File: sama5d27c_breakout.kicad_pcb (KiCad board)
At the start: 4 copper layers, 65 parts, among them U1 SAMA5D2x-SIP

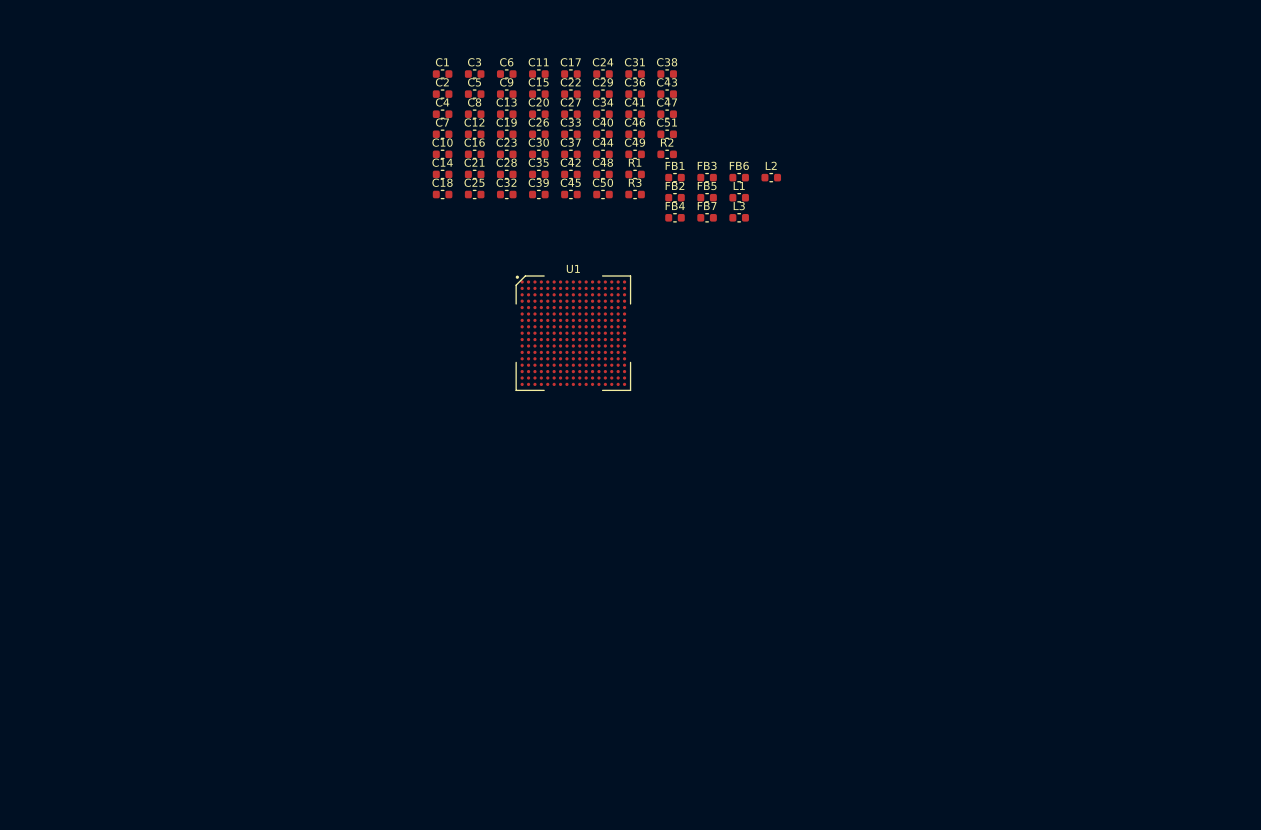
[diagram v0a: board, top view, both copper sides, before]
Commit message: Finish schematic (?), set footprints and start placement
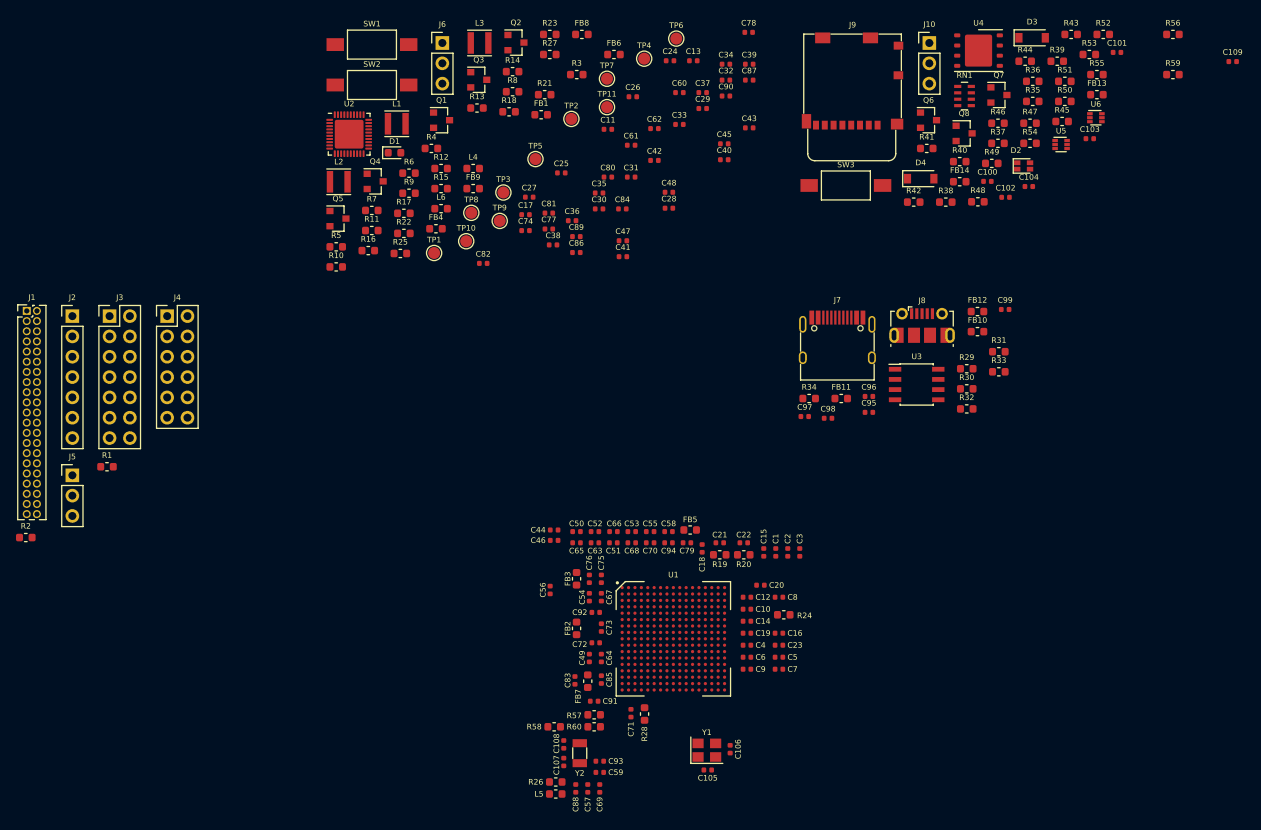
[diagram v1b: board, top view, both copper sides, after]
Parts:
- added C100: 0.1uF, Capacitor_SMD:C_0402_1005Metric, F.Cu at (203.8, 73.5)
- added C101: 10nF, Capacitor_SMD:C_0402_1005Metric, F.Cu at (220.0, 57.4)
- added C102: 10nF, Capacitor_SMD:C_0402_1005Metric, F.Cu at (206.0, 75.5)
- added C103: 10uF, Capacitor_SMD:C_0402_1005Metric, F.Cu at (216.6, 68.2)
- added C104: 10uF, Capacitor_SMD:C_0402_1005Metric, F.Cu at (208.9, 74.2)
- added C105: 12pF, Capacitor_SMD:C_0402_1005Metric, F.Cu at (168.8, 147.1)
- added C106: 12pF, Capacitor_SMD:C_0402_1005Metric, F.Cu at (171.6, 144.5)
- added C107: 12pF, Capacitor_SMD:C_0402_1005Metric, F.Cu at (150.8, 146.1)
- added C108: 12pF, Capacitor_SMD:C_0402_1005Metric, F.Cu at (150.8, 143.9)
- added C109: 10pF, Capacitor_SMD:C_0402_1005Metric, F.Cu at (234.4, 58.5)
- added C52: 1nF, Capacitor_SMD:C_0402_1005Metric, F.Cu at (154.7, 117.3)
- added C53: 1nF, Capacitor_SMD:C_0402_1005Metric, F.Cu at (159.3, 117.3)
- added C54: 1nF, Capacitor_SMD:C_0402_1005Metric, F.Cu at (154.0, 125.5)
- added C55: 1nF, Capacitor_SMD:C_0402_1005Metric, F.Cu at (161.6, 117.3)
- added C56: 10uF, Capacitor_SMD:C_0402_1005Metric, F.Cu at (149.1, 124.6)
- added C57: 1nF, Capacitor_SMD:C_0402_1005Metric, F.Cu at (153.8, 149.4)
- added C58: 1nF, Capacitor_SMD:C_0402_1005Metric, F.Cu at (163.9, 117.3)
- added C59: 1nF, Capacitor_SMD:C_0402_1005Metric, F.Cu at (155.3, 147.4)
- added C60: 0.1uF, Capacitor_SMD:C_0402_1005Metric, F.Cu at (165.3, 62.4)
- added C61: 0.1uF, Capacitor_SMD:C_0402_1005Metric, F.Cu at (159.2, 69.0)
- added C62: 0.1uF, Capacitor_SMD:C_0402_1005Metric, F.Cu at (162.1, 66.9)
- added C63: 0.1uF, Capacitor_SMD:C_0402_1005Metric, F.Cu at (154.7, 118.7)
- added C64: 0.1uF, Capacitor_SMD:C_0402_1005Metric, F.Cu at (155.5, 133.1)
- added C65: 0.1uF, Capacitor_SMD:C_0402_1005Metric, F.Cu at (152.4, 118.7)
- added C66: 0.1uF, Capacitor_SMD:C_0402_1005Metric, F.Cu at (157.0, 117.3)
- added C67: 0.1uF, Capacitor_SMD:C_0402_1005Metric, F.Cu at (155.5, 125.5)
- added C68: 0.1uF, Capacitor_SMD:C_0402_1005Metric, F.Cu at (159.3, 118.7)
- added C69: 0.1uF, Capacitor_SMD:C_0402_1005Metric, F.Cu at (155.3, 149.4)
- added C70: 0.1uF, Capacitor_SMD:C_0402_1005Metric, F.Cu at (161.6, 118.7)
- added C71: 0.1uF, Capacitor_SMD:C_0402_1005Metric, F.Cu at (159.2, 140.0)
- added C72: 0.1uF, Capacitor_SMD:C_0402_1005Metric, F.Cu at (154.8, 131.2)
- added C73: 0.1uF, Capacitor_SMD:C_0402_1005Metric, F.Cu at (155.5, 129.3)
- added C74: 0.1uF, Capacitor_SMD:C_0402_1005Metric, F.Cu at (146.0, 79.7)
- added C75: 0.1uF, Capacitor_SMD:C_0402_1005Metric, F.Cu at (155.5, 123.2)
- added C76: 0.1uF, Capacitor_SMD:C_0402_1005Metric, F.Cu at (154.0, 123.2)
- added C77: 0.1uF, Capacitor_SMD:C_0402_1005Metric, F.Cu at (148.9, 79.5)
- added C78: 0.1uF, Capacitor_SMD:C_0402_1005Metric, F.Cu at (173.9, 54.9)
- added C79: 0.1uF, Capacitor_SMD:C_0402_1005Metric, F.Cu at (166.2, 118.7)
- added C80: 0.1uF, Capacitor_SMD:C_0402_1005Metric, F.Cu at (156.3, 73.0)
- added C81: 0.1uF, Capacitor_SMD:C_0402_1005Metric, F.Cu at (148.9, 77.5)
- added C82: 4.7uF, Capacitor_SMD:C_0402_1005Metric, F.Cu at (140.7, 83.8)
- added C83: 0.1uF, Capacitor_SMD:C_0402_1005Metric, F.Cu at (152.2, 135.9)
- added C84: 4.7uF, Capacitor_SMD:C_0402_1005Metric, F.Cu at (158.1, 77.0)
- added C85: 0.1uF, Capacitor_SMD:C_0402_1005Metric, F.Cu at (155.5, 135.8)
- added C86: 0.1uF, Capacitor_SMD:C_0402_1005Metric, F.Cu at (152.4, 82.4)
- added C87: 0.1uF, Capacitor_SMD:C_0402_1005Metric, F.Cu at (174.0, 60.9)
- added C88: 4.7uF, Capacitor_SMD:C_0402_1005Metric, F.Cu at (152.3, 149.4)
- added C89: 0.1uF, Capacitor_SMD:C_0402_1005Metric, F.Cu at (152.4, 80.4)
- added C90: 4.7uF, Capacitor_SMD:C_0402_1005Metric, F.Cu at (171.1, 62.9)
- added C91: 0.1uF, Capacitor_SMD:C_0402_1005Metric, F.Cu at (154.6, 138.5)
- added C92: 0.1uF, Capacitor_SMD:C_0402_1005Metric, F.Cu at (154.8, 127.4)
- added C93: 0.1uF, Capacitor_SMD:C_0402_1005Metric, F.Cu at (155.3, 146.0)
- added C94: 0.1uF, Capacitor_SMD:C_0402_1005Metric, F.Cu at (163.9, 118.7)
- added C95: 20pF, Capacitor_SMD:C_0402_1005Metric, F.Cu at (188.9, 102.4)
- added C96: 0.1uF, Capacitor_SMD:C_0402_1005Metric, F.Cu at (188.9, 100.4)
- added C97: 0.1uF, Capacitor_SMD:C_0402_1005Metric, F.Cu at (180.9, 102.9)
- added C98: 10uF, Capacitor_SMD:C_0402_1005Metric, F.Cu at (183.8, 103.1)
- added C99: 0.1uF, Capacitor_SMD:C_0402_1005Metric, F.Cu at (206.0, 89.5)
- added D1: LED_CHARGE, LED_SMD:LED_0603_1608Metric, F.Cu at (129.6, 69.9)
- added D2: LED_ARGB, LED_SMD_Extra:LED_RGB_0606_1616Metric, F.Cu at (208.3, 71.6)
- added D3: 1N4148W, Diode_SMD:D_SOD-123, F.Cu at (209.3, 55.6)
- added D4: 1N4148W, Diode_SMD:D_SOD-123, F.Cu at (195.4, 73.2)
- added FB10: BLM18PG300SN1D, Inductor_SMD:L_0603_1608Metric, F.Cu at (202.5, 92.3)
- added FB11: BLM18PG300SN1D, Inductor_SMD:L_0603_1608Metric, F.Cu at (185.5, 100.7)
- added FB12: BLM18PG300SN1D, Inductor_SMD:L_0603_1608Metric, F.Cu at (202.5, 89.8)
- added FB13: BLM18PG300SN1D, Inductor_SMD:L_0603_1608Metric, F.Cu at (217.4, 62.7)
- added FB14: BLM18PG300SN1D, Inductor_SMD:L_0603_1608Metric, F.Cu at (200.3, 73.6)
- added FB8: BLM18PG300SN1D, Inductor_SMD:L_0603_1608Metric, F.Cu at (153.1, 55.2)
- added FB9: BLM18PG300SN1D, Inductor_SMD:L_0603_1608Metric, F.Cu at (139.5, 74.4)
- added J1: Conn_LCD, Connector_PinHeader_1.27mm:PinHeader_2x21_P1.27mm_Vertical, F.Cu at (83.7, 89.7)
- added J10: Conn_Speaker, Connector_PinHeader_2.54mm:PinHeader_1x03_P2.54mm_Vertical, F.Cu at (196.5, 56.2)
- added J2: Conn_JTAG, Connector_PinHeader_2.54mm:PinHeader_1x07_P2.54mm_Vertical, F.Cu at (89.4, 90.4)
- added J3: Conn_SDMMC0, Connector_PinHeader_2.54mm:PinHeader_2x07_P2.54mm_Vertical, F.Cu at (94.0, 90.4)
- added J4: Conn_FLEXCOM3_4, Connector_PinHeader_2.54mm:PinHeader_2x06_P2.54mm_Vertical, F.Cu at (101.2, 90.4)
- added J5: Conn_DBGU, Connector_PinHeader_2.54mm:PinHeader_1x03_P2.54mm_Vertical, F.Cu at (89.4, 110.3)
- added J6: Conn_BAT, Connector_PinHeader_2.54mm:PinHeader_1x03_P2.54mm_Vertical, F.Cu at (135.6, 56.2)
- added J7: USB_C_Receptacle_USB2.0, Connector_USB_Extra:USB_C_Receptacle_GT-USB-7010, F.Cu at (185.0, 93.7)
- added J8: USB_B_Micro, Connector_USB:USB_Micro-B_Molex-105017-0001, F.Cu at (195.6, 91.5)
- added J9: Micro_SD_Card_Det, Connector_Card_Extra:microSD_HC_Molex_104031-0811, F.Cu at (186.9, 61.0)
- added L4: MLZ1608N100L, Inductor_SMD:L_0603_1608Metric, F.Cu at (139.5, 71.9)
- added L5: MLZ1608N100L, Inductor_SMD:L_0603_1608Metric, F.Cu at (149.8, 150.1)
- added L6: MLZ1608N100L, Inductor_SMD:L_0603_1608Metric, F.Cu at (135.5, 76.9)
- added Q1: BSS138, Package_TO_SOT_SMD:SOT-23, F.Cu at (135.5, 65.9)
- added Q2: BSS138, Package_TO_SOT_SMD:SOT-23, F.Cu at (144.8, 56.2)
- added Q3: BSS138, Package_TO_SOT_SMD:SOT-23, F.Cu at (140.2, 60.8)
- added Q4: BSS138, Package_TO_SOT_SMD:SOT-23, F.Cu at (127.2, 73.5)
- added Q5: BSS138, Package_TO_SOT_SMD:SOT-23, F.Cu at (122.6, 78.2)
- added Q6: BSS138, Package_TO_SOT_SMD:SOT-23, F.Cu at (196.4, 65.9)
- added Q7: BSS138, Package_TO_SOT_SMD:SOT-23, F.Cu at (205.2, 62.7)
- added Q8: BSS138, Package_TO_SOT_SMD:SOT-23, F.Cu at (200.8, 67.5)
- added R10: 100K, Resistor_SMD:R_0603_1608Metric, F.Cu at (122.4, 84.2)
- added R11: 10K, Resistor_SMD:R_0603_1608Metric, F.Cu at (126.8, 79.7)
- added R12: 10K, Resistor_SMD:R_0603_1608Metric, F.Cu at (135.5, 71.9)
- added R13: 49.9K, Resistor_SMD:R_0603_1608Metric, F.Cu at (140.0, 64.4)
- added R14: 2.43K, Resistor_SMD:R_0603_1608Metric, F.Cu at (144.4, 59.8)
- added R15: 100R, Resistor_SMD:R_0603_1608Metric, F.Cu at (135.5, 74.4)
- added R16: 100R, Resistor_SMD:R_0603_1608Metric, F.Cu at (126.4, 82.2)
- added R17: 100R, Resistor_SMD:R_0603_1608Metric, F.Cu at (130.8, 77.5)
- added R18: 10K, Resistor_SMD:R_0603_1608Metric, F.Cu at (144.0, 64.8)
- added R19: 1.5K, Resistor_SMD:R_0603_1608Metric, F.Cu at (170.3, 120.2)
- added R20: 1.5K, Resistor_SMD:R_0603_1608Metric, F.Cu at (173.3, 120.2)
- added R21: 100R, Resistor_SMD:R_0603_1608Metric, F.Cu at (148.4, 62.7)
- added R22: 2.2M, Resistor_SMD:R_0603_1608Metric, F.Cu at (130.8, 80.0)
- added R23: 1.5M, Resistor_SMD:R_0603_1608Metric, F.Cu at (149.1, 55.2)
- added R24: 0R, Resistor_SMD:R_0603_1608Metric, F.Cu at (178.3, 127.7)
- added R25: 2.2R, Resistor_SMD:R_0603_1608Metric, F.Cu at (130.4, 82.5)
- added R26: 2.2R, Resistor_SMD:R_0603_1608Metric, F.Cu at (149.8, 148.6)
- added R27: 2.2R, Resistor_SMD:R_0603_1608Metric, F.Cu at (149.1, 57.7)
- added R28: 0R, Resistor_SMD:R_0603_1608Metric, F.Cu at (160.9, 140.1)
- added R29: 5.1K, Resistor_SMD:R_0603_1608Metric, F.Cu at (201.2, 96.9)
- added R30: 5.1K, Resistor_SMD:R_0603_1608Metric, F.Cu at (201.2, 99.5)
- added R31: 100K, Resistor_SMD:R_0603_1608Metric, F.Cu at (205.2, 94.8)
- added R32: 200K, Resistor_SMD:R_0603_1608Metric, F.Cu at (201.2, 102.0)
- added R33: 10K, Resistor_SMD:R_0603_1608Metric, F.Cu at (205.2, 97.3)
- added R34: 10K, Resistor_SMD:R_0603_1608Metric, F.Cu at (181.5, 100.7)
- added R35: 10K, Resistor_SMD:R_0603_1608Metric, F.Cu at (209.4, 63.5)
- added R36: 10K, Resistor_SMD:R_0603_1608Metric, F.Cu at (209.4, 61.0)
- added R37: 100R, Resistor_SMD:R_0603_1608Metric, F.Cu at (205.1, 68.8)
- added R38: 10K, Resistor_SMD:R_0603_1608Metric, F.Cu at (198.6, 76.1)
- added R39: 27R, Resistor_SMD:R_0603_1608Metric, F.Cu at (212.5, 58.5)
- added R4: 100K, Resistor_SMD:R_0603_1608Metric, F.Cu at (134.3, 69.4)
- added R40: 27R, Resistor_SMD:R_0603_1608Metric, F.Cu at (200.3, 71.1)
- added R41: 27R, Resistor_SMD:R_0603_1608Metric, F.Cu at (196.2, 69.4)
- added R42: 27R, Resistor_SMD:R_0603_1608Metric, F.Cu at (194.5, 76.1)
- added R43: 27R, Resistor_SMD:R_0603_1608Metric, F.Cu at (214.2, 55.2)
- added R44: 27R, Resistor_SMD:R_0603_1608Metric, F.Cu at (208.5, 58.5)
- added R45: 10K, Resistor_SMD:R_0603_1608Metric, F.Cu at (213.1, 66.0)
- added R46: 27R, Resistor_SMD:R_0603_1608Metric, F.Cu at (205.1, 66.3)
- added R47: 27R, Resistor_SMD:R_0603_1608Metric, F.Cu at (209.1, 66.3)
- added R48: 27R, Resistor_SMD:R_0603_1608Metric, F.Cu at (202.6, 76.1)
- added R49: 27R, Resistor_SMD:R_0603_1608Metric, F.Cu at (204.3, 71.3)
- added R5: 100K, Resistor_SMD:R_0603_1608Metric, F.Cu at (122.4, 81.7)
- added R50: 10K, Resistor_SMD:R_0603_1608Metric, F.Cu at (213.4, 63.5)
- added R51: 0R, Resistor_SMD:R_0603_1608Metric, F.Cu at (213.4, 61.0)
- added R52: 10K, Resistor_SMD:R_0603_1608Metric, F.Cu at (218.2, 55.2)
- added R53: 10K, Resistor_SMD:R_0603_1608Metric, F.Cu at (216.5, 57.7)
- added R54: 10K, Resistor_SMD:R_0603_1608Metric, F.Cu at (209.1, 68.8)
- added R55: 10K, Resistor_SMD:R_0603_1608Metric, F.Cu at (217.4, 60.2)
- added R56: 100R, Resistor_SMD:R_0603_1608Metric, F.Cu at (226.9, 55.2)
- added R57: 100R, Resistor_SMD:R_0603_1608Metric, F.Cu at (154.6, 140.2)
- added R58: 10K, Resistor_SMD:R_0603_1608Metric, F.Cu at (149.6, 141.7)
- added R59: 5.62K, Resistor_SMD:R_0603_1608Metric, F.Cu at (226.9, 60.2)
- added R6: 68K, Resistor_SMD:R_0603_1608Metric, F.Cu at (131.5, 72.5)
- added R60: 100R, Resistor_SMD:R_0603_1608Metric, F.Cu at (154.6, 141.7)
- added R7: 1K, Resistor_SMD:R_0603_1608Metric, F.Cu at (126.8, 77.2)
- added R8: 100K, Resistor_SMD:R_0603_1608Metric, F.Cu at (144.4, 62.3)
- added R9: 49.9K, Resistor_SMD:R_0603_1608Metric, F.Cu at (131.5, 75.0)
- added RN1: 68K, Resistor_SMD:R_Array_Concave_4x0603, F.Cu at (200.9, 62.9)
- added SW1: SW_WAKEUP, Button_Switch_SMD:SW_SPST_FSMSM, F.Cu at (126.8, 56.4)
- added SW2: SW_RESET, Button_Switch_SMD:SW_SPST_FSMSM, F.Cu at (126.8, 61.5)
- added SW3: SW_USR, Button_Switch_SMD:SW_SPST_FSMSM, F.Cu at (186.1, 74.0)
- added TP1: TP_VBUS, TestPoint:TestPoint_Pad_D1.5mm, F.Cu at (134.6, 82.5)
- added TP10: TP_VDDBU, TestPoint:TestPoint_Pad_D1.5mm, F.Cu at (138.6, 81.0)
- added TP11: TP_VDDSDMMC, TestPoint:TestPoint_Pad_D1.5mm, F.Cu at (156.2, 64.2)
- added TP2: TP_5V, TestPoint:TestPoint_Pad_D1.5mm, F.Cu at (151.8, 65.7)
- added TP3: TP_1.35V, TestPoint:TestPoint_Pad_D1.5mm, F.Cu at (143.3, 74.9)
- added TP4: TP_1.2V, TestPoint:TestPoint_Pad_D1.5mm, F.Cu at (160.9, 58.2)
- added TP5: TP_3.3V, TestPoint:TestPoint_Pad_D1.5mm, F.Cu at (147.3, 70.7)
- added TP6: TP_VDDFUSE, TestPoint:TestPoint_Pad_D1.5mm, F.Cu at (164.9, 55.7)
- added TP7: TP_3.3VP, TestPoint:TestPoint_Pad_D1.5mm, F.Cu at (156.2, 60.7)
- added TP8: TP_VDD_LED, TestPoint:TestPoint_Pad_D1.5mm, F.Cu at (139.2, 77.5)
- added TP9: TP_VDDSDHC1V8, TestPoint:TestPoint_Pad_D1.5mm, F.Cu at (142.8, 78.5)
- added U2: ACT8945A, Package_DFN_QFN:QFN-40-1EP_5x5mm_P0.4mm_EP3.6x3.6mm, F.Cu at (124.0, 67.6)
- added U3: MIC2025, Package_SO:SOIC-8_3.9x4.9mm_P1.27mm, F.Cu at (194.9, 98.9)
- added U4: IS25LP128F, Package_SON:WSON-8-1EP_6x5mm_P1.27mm_EP3.4x4mm, F.Cu at (202.6, 57.2)
- added U5: DMC2450, Package_TO_SOT_SMD:SOT-563, F.Cu at (213.0, 68.9)
- added U6: DMC2450, Package_TO_SOT_SMD:SOT-563, F.Cu at (217.3, 65.6)
- added Y1: TSX-3225 24MHz, Crystal:Crystal_SMD_3225-4Pin_3.2x2.5mm, F.Cu at (168.7, 144.6)
- added Y2: 32kHz, Crystal:Crystal_SMD_3215-2Pin_3.2x1.5mm, F.Cu at (152.8, 145.0)
- C1, C13, C3: value 10uF -> 0.1uF; footprint Capacitor_SMD:C_0603_1608Metric -> Capacitor_SMD:C_0402_1005Metric
- C10, C11, C12, C14, C16, C2, C4, C5, C6, C7, C8, C9: value 1nF -> 0.1uF; footprint Capacitor_SMD:C_0603_1608Metric -> Capacitor_SMD:C_0402_1005Metric
- C15: value 1nF -> 2.2uF; footprint Capacitor_SMD:C_0603_1608Metric -> Capacitor_SMD:C_0402_1005Metric
- C17, C20, C24: value 0.1uF -> 2.2uF; footprint Capacitor_SMD:C_0603_1608Metric -> Capacitor_SMD:C_0402_1005Metric
- C18, C30, C31, C32, C33, C34: value 0.1uF -> 4.7uF; footprint Capacitor_SMD:C_0603_1608Metric -> Capacitor_SMD:C_0402_1005Metric
- C19, C21, C22, C23, C29, C37, C40, C43: footprint Capacitor_SMD:C_0603_1608Metric -> Capacitor_SMD:C_0402_1005Metric
- C25, C27, C28, C35, C36, C38, C42, C44, C46: value 0.1uF -> 10uF; footprint Capacitor_SMD:C_0603_1608Metric -> Capacitor_SMD:C_0402_1005Metric
- C26: value 0.1uF -> 47nF; footprint Capacitor_SMD:C_0603_1608Metric -> Capacitor_SMD:C_0402_1005Metric
- C39, C41: value 4.7uF -> 10uF; footprint Capacitor_SMD:C_0603_1608Metric -> Capacitor_SMD:C_0402_1005Metric
- C45, C47: value 4.7uF -> 1nF; footprint Capacitor_SMD:C_0603_1608Metric -> Capacitor_SMD:C_0402_1005Metric
- C48, C49, C50, C51: value 0.1uF -> 1nF; footprint Capacitor_SMD:C_0603_1608Metric -> Capacitor_SMD:C_0402_1005Metric
- FB1: value BLM03AX100SZ1 -> BLM18PG181SN1D
- FB2, FB3, FB4, FB5, FB6, FB7: value BLM03AX100SZ1 -> BLM18PG300SN1D
- L1, L2, L3: value MLZ1608N100L -> LQM2HPN2R2MG0L; footprint Inductor_SMD:L_0603_1608Metric -> Inductor_SMD:L_Taiyo-Yuden_MD-3030
- R1, R2: value 2.2R -> 4.7K
- R3: value 2.2R -> 100K
- moved R2 93.4 mm to (83.6, 118.0)
- moved C5 80.0 mm to (177.7, 133.0), turned to 180 degrees
- moved C7 79.0 mm to (177.7, 134.5), turned to 180 degrees
- moved C6 78.8 mm to (173.7, 133.0), turned to 180 degrees
- moved C9 77.9 mm to (173.7, 134.5), turned to 180 degrees
- moved C4 76.5 mm to (173.7, 131.5), turned to 180 degrees
- moved R1 75.4 mm to (93.7, 109.2)
- moved C1 72.9 mm to (177.3, 119.9), turned to 270 degrees
- moved C3 72.3 mm to (180.3, 119.9), turned to 270 degrees
- moved C2 71.7 mm to (178.8, 119.9), turned to 270 degrees
- moved C8 71.4 mm to (177.7, 125.5), turned to 180 degrees
- moved C16 70.9 mm to (177.7, 130.0), turned to 180 degrees
- moved C23 70.2 mm to (177.7, 131.5), turned to 180 degrees
- moved C19 69.2 mm to (173.7, 130.0), turned to 180 degrees
- moved C10 68.4 mm to (173.7, 127.0), turned to 180 degrees
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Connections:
- C1 pad 2: VDDIODDR -> +1V35
- C10 pad 2: VDDIODDR -> +1V35
- C11 pad 1: GND -> Net-(C11-Pad1)
- C11 pad 2: VDDCORE -> Net-(C11-Pad2)
- C12 pad 2: VDDIODDR -> +1V35
- C13 pad 1: GND -> +5V
- C13 pad 2: +3V3 -> Net-(C13-Pad2)
- C14 pad 2: VDDCORE -> +1V35
- C15 pad 2: VDDIODDR -> +1V35
- C16 pad 2: VDDCORE -> +1V35
- C17 pad 2: VDDIODDR -> +1V35
- C18 pad 1: GND -> +1V35
- C18 pad 2: VDDCORE -> GND
- C19 pad 2: VDDIODDR -> +1V35
- C2 pad 2: VDDIODDR -> +1V35
- C20 pad 2: VDDCORE -> +1V35
- C21 pad 1: GND -> Net-(C21-Pad1)
- C21 pad 2: VDDIODDR -> +1V35
- C22 pad 2: VDDCORE -> Net-(C21-Pad1)
- C23 pad 2: VDDIODDR -> +1V35
- C24 pad 2: VDDCORE -> +1V35
- C25 pad 1: GND -> VBUS
- C25 pad 2: VDDIODDR -> GND
- C26 pad 1: GND -> Net-(C26-Pad1)
- C26 pad 2: VDDCORE -> GND
- C27 pad 2: VDDIODDR -> +5V
- C28 pad 1: VDDBU -> GND
- C28 pad 2: GND -> +5V
- C29 pad 1: Net-(C29-Pad1) -> GND
- C29 pad 2: GND -> +5V
- C3 pad 2: VDDCORE -> +1V35
- C30 pad 1: Net-(C29-Pad1) -> GND
- C30 pad 2: GND -> +5V
- C31 pad 1: Net-(C29-Pad1) -> GND
- C31 pad 2: GND -> VDDFUSE
- C32 pad 1: Net-(C32-Pad1) -> GND
- C32 pad 2: GND -> +3.3VP
- C33 pad 1: Net-(C32-Pad1) -> GND
- C33 pad 2: GND -> /Power/VDD_LED
- C34 pad 1: Net-(C34-Pad1) -> GND
- C34 pad 2: GND -> /Power/VDDSDHC1V8
- C35 pad 1: Net-(C34-Pad1) -> GND
- C35 pad 2: GND -> +1V35
- C36 pad 1: Net-(C36-Pad1) -> GND
- C36 pad 2: GND -> +1V35
- C37 pad 1: Net-(C37-Pad1) -> GND
- C37 pad 2: GND -> +1V35
- C38 pad 1: VDDFUSE -> GND
- C38 pad 2: GND -> +1V2
- C39 pad 1: Net-(C39-Pad1) -> GND
- C39 pad 2: GND -> +1V2
- C4 pad 2: VDDIODDR -> +1V35
- C40 pad 1: Net-(C39-Pad1) -> GND
- C40 pad 2: GND -> +1V2
- C41 pad 1: Net-(C41-Pad1) -> GND
- C41 pad 2: GND -> +3V3
- C42 pad 1: Net-(C41-Pad1) -> GND
- C42 pad 2: GND -> +3V3
- C43 pad 1: Net-(C43-Pad1) -> GND
- C43 pad 2: GNDS -> +3V3
- C44 pad 1: VDDSDMMC -> GND
- C44 pad 2: GND -> +1V35
- C45 pad 1: Net-(C45-Pad1) -> GND
- C45 pad 2: GND -> +1V35
- C46 pad 1: Net-(C45-Pad1) -> GND
- C46 pad 2: GND -> +1V2
- C47 pad 1: Net-(C47-Pad1) -> GND
- C47 pad 2: GND -> +1V35
- C48 pad 1: Net-(C47-Pad1) -> GND
- C48 pad 2: GND -> +1V2
- C49 pad 1: VDDISC -> GND
- C49 pad 2: GND -> +1V35
- C5 pad 2: VDDCORE -> +1V35
- C50 pad 2: VDDCORE -> +1V2
- C51 pad 2: VDDIODDR -> +1V35
- C6 pad 2: VDDIODDR -> +1V35
- C7 pad 2: VDDCORE -> +1V35
- C8 pad 2: VDDIODDR -> +1V35
- C9 pad 2: VDDCORE -> +1V35
- FB1 pad 1: +3V3 -> Net-(FB1-Pad1)
- FB1 pad 2: Net-(C29-Pad1) -> /Power/VDDSDHC1V8
- FB2 pad 1: +3V3 -> +3.3VP
- FB2 pad 2: Net-(C32-Pad1) -> VDDA
- FB3 pad 2: Net-(C34-Pad1) -> Net-(C75-Pad1)
- FB4 pad 2: Net-(C36-Pad1) -> Net-(C77-Pad1)
- FB5 pad 1: VDDCORE -> +3V3
- FB5 pad 2: Net-(C37-Pad1) -> Net-(C79-Pad1)
- FB6 pad 1: VDDCORE -> +1V2
- FB6 pad 2: Net-(C41-Pad1) -> Net-(C80-Pad1)
- FB7 pad 1: +3V3 -> +1V2
- FB7 pad 2: Net-(C43-Pad1) -> Net-(C84-Pad1)
- L1 pad 1: Net-(L1-Pad1) -> +1V35
- L1 pad 2: Net-(C39-Pad1) -> Net-(L1-Pad2)
- L2 pad 1: Net-(L2-Pad1) -> +1V2
- L2 pad 2: Net-(C45-Pad1) -> Net-(L2-Pad2)
- L3 pad 1: Net-(L3-Pad1) -> +3V3
- L3 pad 2: Net-(C47-Pad1) -> Net-(L3-Pad2)
- R1 pad 1: Net-(L1-Pad1) -> +3V3
- R1 pad 2: +3V3 -> /LCD_TWCK
- R2 pad 1: Net-(L2-Pad1) -> +3V3
- R2 pad 2: VDDCORE -> /LCD_TWD
- R3 pad 1: Net-(L3-Pad1) -> /Power/nPBSTAT
- R3 pad 2: +3V3 -> +5V
- U1 pad A10: Net-(U1-PadA10) -> /QSPI1_SCK
- U1 pad A11: Net-(U1-PadA11) -> /FLEXCOM4_IO3
- U1 pad A16: Net-(U1-PadA16) -> +1V35
- U1 pad A17: Net-(U1-PadA17) -> GND
- U1 pad A3: Net-(U1-PadA3) -> /LCD_DAT14
- U1 pad A4: Net-(U1-PadA4) -> /LCD_DAT9
- U1 pad A5: Net-(U1-PadA5) -> /LCD_DAT7
- U1 pad A6: Net-(U1-PadA6) -> /LCD_DAT3
- U1 pad A7: Net-(U1-PadA7) -> /LCD_DAT0
- U1 pad A8: Net-(U1-PadA8) -> /QSPI1_IO3
- U1 pad A9: Net-(U1-PadA9) -> /QSPI1_CS
- U1 pad B16: Net-(U1-PadA16) -> +1V35
- U1 pad B17: Net-(U1-PadA17) -> GND
- U1 pad B2: Net-(U1-PadB2) -> /PMIC_LBO
- U1 pad B3: Net-(U1-PadB3) -> /LCD_DAT12
- U1 pad B4: Net-(U1-PadB4) -> /LCD_DAT8
- U1 pad B5: Net-(U1-PadB5) -> /LCD_DAT5
- U1 pad B6: Net-(U1-PadB6) -> /LCD_DAT1
- U1 pad B7: Net-(U1-PadB7) -> /CLASSD_R3
- U1 pad B8: Net-(U1-PadB8) -> /CLASSD_R2
- U1 pad B9: Net-(U1-PadB9) -> /FLEXCOM4_IO1
- U1 pad C16: Net-(U1-PadA16) -> +1V35
- U1 pad C17: Net-(U1-PadA17) -> GND
- U1 pad C2: Net-(U1-PadC2) -> /LCD_DAT19
- U1 pad C3: Net-(U1-PadC3) -> /LCD_DAT11
- U1 pad C4: Net-(U1-PadC4) -> /LCD_DAT6
- U1 pad C5: Net-(U1-PadC5) -> /LCD_DAT2
- U1 pad C6: Net-(U1-PadC6) -> /QSPI1_IO2
- U1 pad C7: Net-(U1-PadC7) -> /CLASSD_R1
- U1 pad C8: Net-(U1-PadC8) -> /CLASSD_R0
- U1 pad C9: Net-(U1-PadC9) -> /IRQ1
- U1 pad D1: Net-(U1-PadD1) -> /FLEXCOM3_IO1
- U1 pad D15: Net-(U1-PadA17) -> GND
- U1 pad D16: Net-(U1-PadA16) -> +1V35
- U1 pad D2: Net-(U1-PadD2) -> /LCD_DAT17
- U1 pad D3: Net-(U1-PadD3) -> /LCD_DAT10
- U1 pad D4: Net-(C32-Pad1) -> Net-(C75-Pad1)
- U1 pad D5: Net-(U1-PadD5) -> /QSPI1_IO0
- U1 pad D7: VDDCORE -> +1V2
- U1 pad D8: Net-(U1-PadD8) -> /DBGU_RX
- U1 pad D9: Net-(C36-Pad1) -> Net-(C79-Pad1)
- U1 pad E1: Net-(U1-PadE1) -> /FLEXCOM3_IO3
- U1 pad E11: VDDIODDR -> +1V35
- U1 pad E14: Net-(U1-PadA17) -> GND
- U1 pad E15: Net-(U1-PadA16) -> +1V35
- U1 pad E16: Net-(U1-PadE16) -> +1V35
- U1 pad E17: Net-(U1-PadE17) -> GND
- U1 pad E2: Net-(U1-PadE2) -> /LCD_DAT13
- U1 pad E4: Net-(U1-PadE4) -> /LCD_DAT4
- U1 pad E5: Net-(U1-PadE5) -> /QSPI1_IO1
- U1 pad E6: Net-(U1-PadE6) -> /FLEXCOM4_IO2
- U1 pad E7: Net-(U1-PadE7) -> /FLEXCOM4_IO4
- U1 pad E8: VDDIODDR -> +1V35
- U1 pad E9: VDDCORE -> +1V2
- U1 pad F1: Net-(U1-PadF1) -> /FLEXCOM3_IO4
- U1 pad F11: Net-(U1-PadF11) -> Net-(C21-Pad1)
- U1 pad F15: Net-(U1-PadF15) -> +1V35
- U1 pad F16: Net-(U1-PadF16) -> GND
- U1 pad F17: Net-(U1-PadA17) -> GND
- U1 pad F3: Net-(C32-Pad1) -> Net-(C75-Pad1)
- U1 pad F4: Net-(U1-PadF4) -> /LCD_DAT16
- U1 pad F5: Net-(U1-PadF5) -> /LED_GREEN
- U1 pad F6: Net-(U1-PadF6) -> /FLEXCOM4_IO0
- U1 pad G12: VDDIODDR -> +1V35
- U1 pad G15: Net-(U1-PadF15) -> +1V35
- U1 pad G16: Net-(U1-PadF16) -> GND
- U1 pad G17: Net-(U1-PadA16) -> +1V35
- U1 pad G3: Net-(U1-PadG3) -> /LCD_DAT15
- U1 pad G4: Net-(U1-PadG4) -> /PMIC_IRQ
- U1 pad G7: Net-(U1-PadG7) -> /LCD_DAT20
- U1 pad G8: Net-(U1-PadG8) -> /LCD_DAT18
- U1 pad G9: Net-(U1-PadG9) -> /FLEXCOM3_IO2
- U1 pad H1: Net-(U1-PadH1) -> /LCD_TWCK
- U1 pad H10: VDDIODDR -> +1V35
- U1 pad H15: Net-(U1-PadF15) -> +1V35
- U1 pad H16: Net-(U1-PadF16) -> GND
- U1 pad H17: Net-(U1-PadA17) -> GND
- U1 pad H2: VDDCORE -> +1V2
- U1 pad H3: VDDISC -> Net-(C92-Pad1)
- U1 pad H4: Net-(U1-PadH4) -> /FLEXCOM3_IO0
- U1 pad H7: Net-(U1-PadH7) -> /LCD_TWD
- U1 pad H8: Net-(U1-PadH8) -> /IRQ2
- U1 pad J1: Net-(U1-PadJ1) -> /DBGU_TX
- U1 pad J10: Net-(U1-PadF11) -> Net-(C21-Pad1)
- U1 pad J15: Net-(U1-PadF15) -> +1V35
- U1 pad J16: Net-(U1-PadF16) -> GND
- U1 pad J17: Net-(U1-PadA16) -> +1V35
- U1 pad J5: Net-(C29-Pad1) -> VDDA
- U1 pad J8: VDDIODDR -> +1V35
- U1 pad K15: Net-(U1-PadF15) -> +1V35
- U1 pad K16: Net-(U1-PadF16) -> GND
- U1 pad K17: Net-(U1-PadF16) -> GND
- U1 pad K4: Net-(C29-Pad1) -> VDDA
- U1 pad L10: VDDIODDR -> +1V35
- U1 pad L11: Net-(U1-PadL11) -> /LCD_HSYNC
- U1 pad L12: VDDCORE -> +1V2
- U1 pad L14: VDDIODDR -> +1V35
- U1 pad L15: Net-(U1-PadF15) -> +1V35
- U1 pad L16: Net-(U1-PadA16) -> +1V35
- U1 pad L17: Net-(U1-PadA17) -> GND
- U1 pad L2: Net-(U1-PadL2) -> /USBA_VBUS_5V
- U1 pad L3: Net-(U1-PadL3) -> /JTAG_TDI
- U1 pad L6: Net-(U1-PadL6) -> /PMIC_TWCK
- U1 pad L7: Net-(U1-PadL7) -> /JTAG_TCK
- U1 pad L8: Net-(U1-PadL8) -> /USBB_OVERCURR
- U1 pad L9: Net-(U1-PadL9) -> VDDA
- U1 pad M10: Net-(U1-PadM10) -> /LCD_PWM
- U1 pad M11: Net-(U1-PadM11) -> /SPI0_MISO
- U1 pad M13: Net-(U1-PadM13) -> /LCD_DEN
- U1 pad M15: Net-(U1-PadM15) -> /LCD_PCK
- U1 pad M16: Net-(U1-PadM16) -> /LCD_VSYNC
- U1 pad M17: Net-(U1-PadM17) -> /SPI0_SPCK
- U1 pad M2: Net-(U1-PadM2) -> /JTAG_TDO
- U1 pad M4: Net-(C39-Pad1) -> Net-(C82-Pad1)
- U1 pad M7: Net-(C41-Pad1) -> Net-(C84-Pad1)
- U1 pad M9: Net-(U1-PadM9) -> /JTAG_TMS
- U1 pad N10: Net-(U1-PadN10) -> /LCD_DAT21
- U1 pad N11: Net-(U1-PadN11) -> /LCD_DAT22
- U1 pad N12: Net-(C34-Pad1) -> Net-(C77-Pad1)
- U1 pad N14: Net-(U1-PadN14) -> /SPI0_NPCS0
- U1 pad N15: Net-(U1-PadN15) -> /LCD_DISP
- U1 pad N16: Net-(U1-PadN16) -> /SPI0_MOSI
- U1 pad N17: Net-(U1-PadN17) -> /PMIC_CHGLEV
- U1 pad N6: Net-(C47-Pad1) -> Net-(C90-Pad1)
- U1 pad N7: Net-(U1-PadN7) -> /SDMMC0_CDA
- U1 pad N8: VDDSDMMC -> +3V3
- U1 pad N9: Net-(U1-PadN9) -> /LCD_DAT23
- U1 pad P1: Net-(U1-PadP1) -> /PMIC_TWD
- U1 pad P10: Net-(U1-PadP10) -> /SDMMC1_DAT3
- U1 pad P12: Net-(C34-Pad1) -> Net-(C77-Pad1)
- U1 pad P13: Net-(U1-PadP13) -> /LED_BLUE
- U1 pad P14: Net-(U1-PadP14) -> /USR_BTN
- U1 pad P15: Net-(U1-PadP15) -> /SDMMC0_VDDSEL
- U1 pad P16: Net-(U1-PadP16) -> /SDMMC0_CD
- U1 pad P6: Net-(C43-Pad1) -> Net-(C86-Pad1)
- U1 pad P7: VDDCORE -> +1V2
- U1 pad P8: Net-(U1-PadP8) -> /SDMMC0_DAT7
- U1 pad P9: Net-(U1-PadP9) -> /SDMMC1_DAT2
- U1 pad R10: Net-(U1-PadR10) -> /LED_RED
- U1 pad R11: Net-(U1-PadR11) -> /SDMMC0_DAT5
- U1 pad R13: Net-(U1-PadR13) -> /SDMMC1_CD
- U1 pad R14: Net-(U1-PadR14) -> /SDMMC1_CDA
- U1 pad R15: Net-(U1-PadR15) -> /USBB_PWR_EN
- U1 pad R5: Net-(C45-Pad1) -> Net-(C88-Pad1)
- U1 pad R7: Net-(C37-Pad1) -> Net-(C80-Pad1)
- U1 pad R9: Net-(U1-PadR9) -> /SDMMC0_DAT6
- U1 pad T10: Net-(U1-PadT10) -> /USB/A_D-
- U1 pad T11: Net-(U1-PadT11) -> /USB/B_D-
- U1 pad T13: Net-(U1-PadT13) -> /SDMMC0_DAT1
- U1 pad T15: Net-(U1-PadT15) -> /SDMMC1_DAT1
- U1 pad T16: Net-(U1-PadT16) -> /SDMMC1_DAT0
- U1 pad T17: Net-(U1-PadT17) -> /SDMMC1_CK
- U1 pad U10: Net-(U1-PadU10) -> /USB/A_D+
- U1 pad U11: Net-(U1-PadU11) -> /USB/B_D+
- U1 pad U13: Net-(U1-PadU13) -> /SDMMC0_CK
- U1 pad U14: Net-(U1-PadU14) -> /SDMMC0_DAT0
- U1 pad U15: Net-(U1-PadU15) -> /SDMMC0_DAT2
- U1 pad U16: Net-(U1-PadU16) -> /SDMMC0_DAT3
- U1 pad U17: Net-(U1-PadU17) -> /SDMMC0_DAT4
- U1 pad U3: VDDCORE -> +1V2
- U1 pad U5: VDDBU -> +3V3
